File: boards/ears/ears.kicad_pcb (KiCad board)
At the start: 2 copper layers, 5 parts, among them J1 Conn_01x02_Male, U1 AZ1117-3.3, U2 SPX2920T-5.0_TO263, U3 ESP32-WROOM-32D

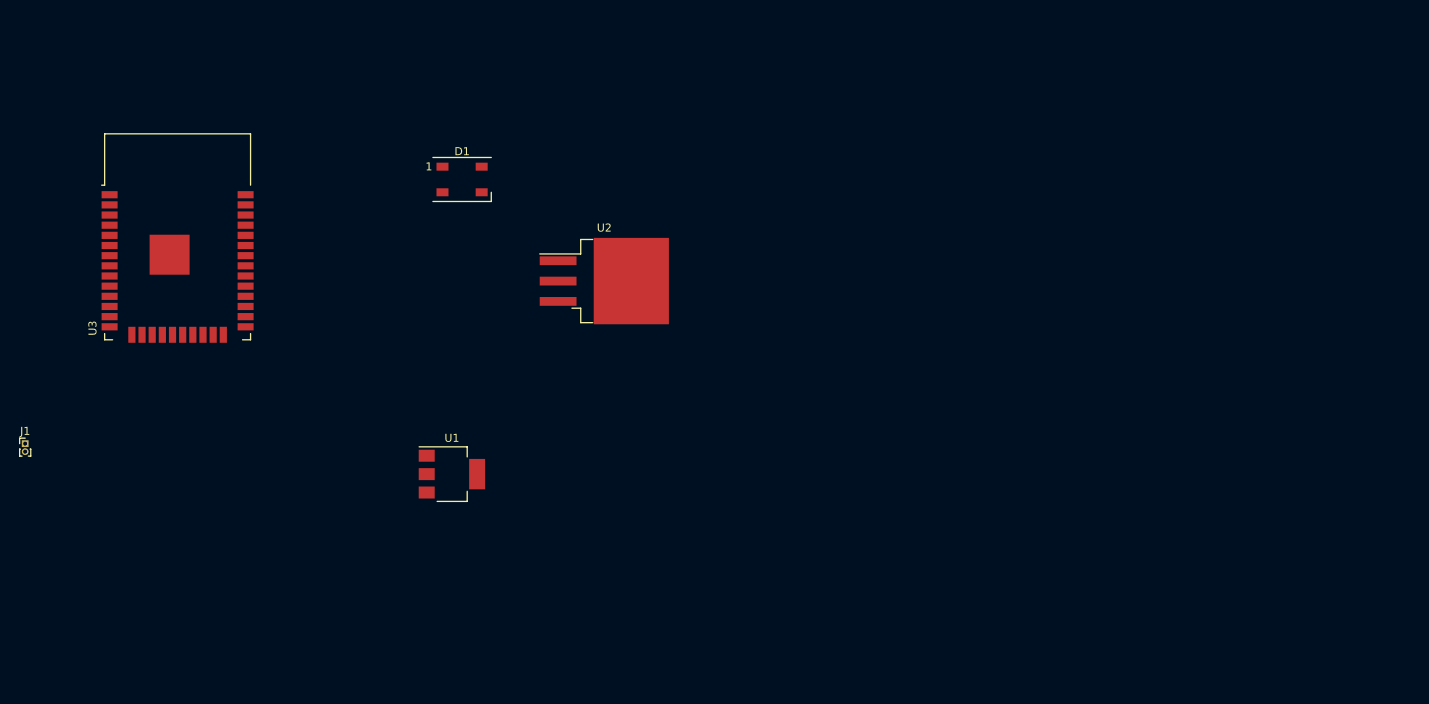
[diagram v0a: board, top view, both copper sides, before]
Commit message: - Ear boards V1
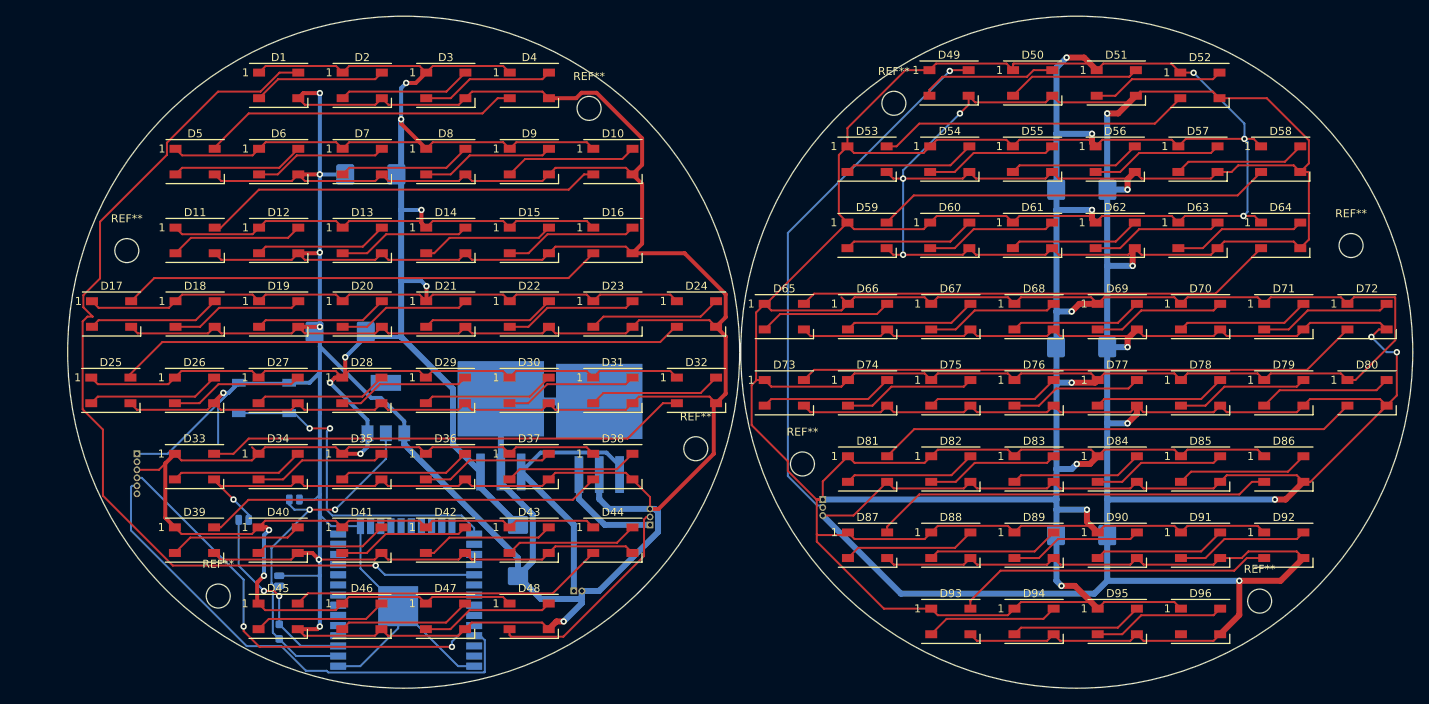
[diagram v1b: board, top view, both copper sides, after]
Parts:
- added C1: 0.1uF, Capacitor_SMD:C_0504_1310Metric_Pad0.83x1.28mm_HandSolder, B.Cu at (43.8, 79.4)
- added C2: 10uF, Capacitor_SMD:C_0504_1310Metric_Pad0.83x1.28mm_HandSolder, B.Cu at (50.2, 76.8)
- added C3: 0.1uF, Capacitor_SMD:C_0504_1310Metric_Pad0.83x1.28mm_HandSolder, B.Cu at (48.3, 87.0)
- added C4: 470uF, Capacitor_Tantalum_SMD:CP_EIA-7343-15_Kemet-W_Pad2.25x2.55mm_HandSolder, B.Cu at (55.9, 55.9)
- added C5: 470uF, Capacitor_Tantalum_SMD:CP_EIA-7343-15_Kemet-W_Pad2.25x2.55mm_HandSolder, B.Cu at (78.1, 83.2)
- added C6: 470uF, Capacitor_Tantalum_SMD:CP_EIA-7343-15_Kemet-W_Pad2.25x2.55mm_HandSolder, B.Cu at (59.7, 36.2)
- added C7: 470uF, Capacitor_Tantalum_SMD:CP_EIA-7343-15_Kemet-W_Pad2.25x2.55mm_HandSolder, B.Cu at (148.6, 57.8)
- added C8: 470uF, Capacitor_Tantalum_SMD:CP_EIA-7343-15_Kemet-W_Pad2.25x2.55mm_HandSolder, B.Cu at (148.6, 38.1)
- added C9: 470uF, Capacitor_Tantalum_SMD:CP_EIA-7343-15_Kemet-W_Pad2.25x2.55mm_HandSolder, B.Cu at (148.6, 81.3)
- added D10: WS2812B, LED_SMD:LED_WS2812B_PLCC4_5.0x5.0mm_P3.2mm, F.Cu at (90.0, 34.6)
- added D11: WS2812B, LED_SMD:LED_WS2812B_PLCC4_5.0x5.0mm_P3.2mm, F.Cu at (37.8, 44.5)
- added D12: WS2812B, LED_SMD:LED_WS2812B_PLCC4_5.0x5.0mm_P3.2mm, F.Cu at (48.2, 44.5)
- added D13: WS2812B, LED_SMD:LED_WS2812B_PLCC4_5.0x5.0mm_P3.2mm, F.Cu at (58.6, 44.5)
- added D14: WS2812B, LED_SMD:LED_WS2812B_PLCC4_5.0x5.0mm_P3.2mm, F.Cu at (69.1, 44.5)
- added D15: WS2812B, LED_SMD:LED_WS2812B_PLCC4_5.0x5.0mm_P3.2mm, F.Cu at (79.5, 44.5)
- added D16: WS2812B, LED_SMD:LED_WS2812B_PLCC4_5.0x5.0mm_P3.2mm, F.Cu at (90.0, 44.5)
- added D17: WS2812B, LED_SMD:LED_WS2812B_PLCC4_5.0x5.0mm_P3.2mm, F.Cu at (27.3, 53.6)
- added D18: WS2812B, LED_SMD:LED_WS2812B_PLCC4_5.0x5.0mm_P3.2mm, F.Cu at (37.8, 53.6)
- added D19: WS2812B, LED_SMD:LED_WS2812B_PLCC4_5.0x5.0mm_P3.2mm, F.Cu at (48.2, 53.6)
- added D2: WS2812B, LED_SMD:LED_WS2812B_PLCC4_5.0x5.0mm_P3.2mm, F.Cu at (58.6, 25.1)
- added D20: WS2812B, LED_SMD:LED_WS2812B_PLCC4_5.0x5.0mm_P3.2mm, F.Cu at (58.6, 53.6)
- added D21: WS2812B, LED_SMD:LED_WS2812B_PLCC4_5.0x5.0mm_P3.2mm, F.Cu at (69.1, 53.6)
- added D22: WS2812B, LED_SMD:LED_WS2812B_PLCC4_5.0x5.0mm_P3.2mm, F.Cu at (79.5, 53.6)
- added D23: WS2812B, LED_SMD:LED_WS2812B_PLCC4_5.0x5.0mm_P3.2mm, F.Cu at (90.0, 53.6)
- added D24: WS2812B, LED_SMD:LED_WS2812B_PLCC4_5.0x5.0mm_P3.2mm, F.Cu at (100.4, 53.6)
- added D25: WS2812B, LED_SMD:LED_WS2812B_PLCC4_5.0x5.0mm_P3.2mm, F.Cu at (27.2, 63.2)
- added D26: WS2812B, LED_SMD:LED_WS2812B_PLCC4_5.0x5.0mm_P3.2mm, F.Cu at (37.7, 63.2)
- added D27: WS2812B, LED_SMD:LED_WS2812B_PLCC4_5.0x5.0mm_P3.2mm, F.Cu at (48.1, 63.2)
- added D28: WS2812B, LED_SMD:LED_WS2812B_PLCC4_5.0x5.0mm_P3.2mm, F.Cu at (58.6, 63.2)
- added D29: WS2812B, LED_SMD:LED_WS2812B_PLCC4_5.0x5.0mm_P3.2mm, F.Cu at (69.0, 63.2)
- added D3: WS2812B, LED_SMD:LED_WS2812B_PLCC4_5.0x5.0mm_P3.2mm, F.Cu at (69.1, 25.1)
- added D30: WS2812B, LED_SMD:LED_WS2812B_PLCC4_5.0x5.0mm_P3.2mm, F.Cu at (79.5, 63.2)
- added D31: WS2812B, LED_SMD:LED_WS2812B_PLCC4_5.0x5.0mm_P3.2mm, F.Cu at (90.0, 63.2)
- added D32: WS2812B, LED_SMD:LED_WS2812B_PLCC4_5.0x5.0mm_P3.2mm, F.Cu at (100.4, 63.2)
- added D33: WS2812B, LED_SMD:LED_WS2812B_PLCC4_5.0x5.0mm_P3.2mm, F.Cu at (37.7, 72.7)
- added D34: WS2812B, LED_SMD:LED_WS2812B_PLCC4_5.0x5.0mm_P3.2mm, F.Cu at (48.1, 72.7)
- added D35: WS2812B, LED_SMD:LED_WS2812B_PLCC4_5.0x5.0mm_P3.2mm, F.Cu at (58.6, 72.7)
- added D36: WS2812B, LED_SMD:LED_WS2812B_PLCC4_5.0x5.0mm_P3.2mm, F.Cu at (69.0, 72.7)
- added D37: WS2812B, LED_SMD:LED_WS2812B_PLCC4_5.0x5.0mm_P3.2mm, F.Cu at (79.5, 72.7)
- added D38: WS2812B, LED_SMD:LED_WS2812B_PLCC4_5.0x5.0mm_P3.2mm, F.Cu at (90.0, 72.7)
- added D39: WS2812B, LED_SMD:LED_WS2812B_PLCC4_5.0x5.0mm_P3.2mm, F.Cu at (37.7, 81.9)
- added D4: WS2812B, LED_SMD:LED_WS2812B_PLCC4_5.0x5.0mm_P3.2mm, F.Cu at (79.5, 25.1)
- added D40: WS2812B, LED_SMD:LED_WS2812B_PLCC4_5.0x5.0mm_P3.2mm, F.Cu at (48.1, 81.9)
- added D41: WS2812B, LED_SMD:LED_WS2812B_PLCC4_5.0x5.0mm_P3.2mm, F.Cu at (58.6, 81.9)
- added D42: WS2812B, LED_SMD:LED_WS2812B_PLCC4_5.0x5.0mm_P3.2mm, F.Cu at (69.0, 81.9)
- added D43: WS2812B, LED_SMD:LED_WS2812B_PLCC4_5.0x5.0mm_P3.2mm, F.Cu at (79.5, 81.9)
- added D44: WS2812B, LED_SMD:LED_WS2812B_PLCC4_5.0x5.0mm_P3.2mm, F.Cu at (90.0, 81.9)
- added D45: WS2812B, LED_SMD:LED_WS2812B_PLCC4_5.0x5.0mm_P3.2mm, F.Cu at (48.1, 91.4)
- added D46: WS2812B, LED_SMD:LED_WS2812B_PLCC4_5.0x5.0mm_P3.2mm, F.Cu at (58.6, 91.4)
- added D47: WS2812B, LED_SMD:LED_WS2812B_PLCC4_5.0x5.0mm_P3.2mm, F.Cu at (69.0, 91.4)
- added D48: WS2812B, LED_SMD:LED_WS2812B_PLCC4_5.0x5.0mm_P3.2mm, F.Cu at (79.5, 91.4)
- added D49: WS2812B, LED_SMD:LED_WS2812B_PLCC4_5.0x5.0mm_P3.2mm, F.Cu at (132.0, 24.8)
- added D5: WS2812B, LED_SMD:LED_WS2812B_PLCC4_5.0x5.0mm_P3.2mm, F.Cu at (37.8, 34.6)
- added D50: WS2812B, LED_SMD:LED_WS2812B_PLCC4_5.0x5.0mm_P3.2mm, F.Cu at (142.4, 24.8)
- added D51: WS2812B, LED_SMD:LED_WS2812B_PLCC4_5.0x5.0mm_P3.2mm, F.Cu at (152.9, 24.8)
- added D52: WS2812B, LED_SMD:LED_WS2812B_PLCC4_5.0x5.0mm_P3.2mm, F.Cu at (163.3, 25.1)
- added D53: WS2812B, LED_SMD:LED_WS2812B_PLCC4_5.0x5.0mm_P3.2mm, F.Cu at (121.7, 34.3)
- added D54: WS2812B, LED_SMD:LED_WS2812B_PLCC4_5.0x5.0mm_P3.2mm, F.Cu at (132.1, 34.3)
- added D55: WS2812B, LED_SMD:LED_WS2812B_PLCC4_5.0x5.0mm_P3.2mm, F.Cu at (142.4, 34.3)
- added D56: WS2812B, LED_SMD:LED_WS2812B_PLCC4_5.0x5.0mm_P3.2mm, F.Cu at (152.8, 34.3)
- added D57: WS2812B, LED_SMD:LED_WS2812B_PLCC4_5.0x5.0mm_P3.2mm, F.Cu at (163.1, 34.3)
- added D58: WS2812B, LED_SMD:LED_WS2812B_PLCC4_5.0x5.0mm_P3.2mm, F.Cu at (173.4, 34.3)
- added D59: WS2812B, LED_SMD:LED_WS2812B_PLCC4_5.0x5.0mm_P3.2mm, F.Cu at (121.7, 43.8)
- added D6: WS2812B, LED_SMD:LED_WS2812B_PLCC4_5.0x5.0mm_P3.2mm, F.Cu at (48.2, 34.6)
- added D60: WS2812B, LED_SMD:LED_WS2812B_PLCC4_5.0x5.0mm_P3.2mm, F.Cu at (132.1, 43.8)
- added D61: WS2812B, LED_SMD:LED_WS2812B_PLCC4_5.0x5.0mm_P3.2mm, F.Cu at (142.4, 43.8)
- added D62: WS2812B, LED_SMD:LED_WS2812B_PLCC4_5.0x5.0mm_P3.2mm, F.Cu at (152.8, 43.8)
- added D63: WS2812B, LED_SMD:LED_WS2812B_PLCC4_5.0x5.0mm_P3.2mm, F.Cu at (163.1, 43.8)
- added D64: WS2812B, LED_SMD:LED_WS2812B_PLCC4_5.0x5.0mm_P3.2mm, F.Cu at (173.4, 43.8)
- added D65: WS2812B, LED_SMD:LED_WS2812B_PLCC4_5.0x5.0mm_P3.2mm, F.Cu at (111.4, 54.0)
- added D66: WS2812B, LED_SMD:LED_WS2812B_PLCC4_5.0x5.0mm_P3.2mm, F.Cu at (121.8, 54.0)
- added D67: WS2812B, LED_SMD:LED_WS2812B_PLCC4_5.0x5.0mm_P3.2mm, F.Cu at (132.2, 54.0)
- added D68: WS2812B, LED_SMD:LED_WS2812B_PLCC4_5.0x5.0mm_P3.2mm, F.Cu at (142.6, 54.0)
- added D69: WS2812B, LED_SMD:LED_WS2812B_PLCC4_5.0x5.0mm_P3.2mm, F.Cu at (153.0, 54.0)
- added D7: WS2812B, LED_SMD:LED_WS2812B_PLCC4_5.0x5.0mm_P3.2mm, F.Cu at (58.6, 34.6)
- added D70: WS2812B, LED_SMD:LED_WS2812B_PLCC4_5.0x5.0mm_P3.2mm, F.Cu at (163.4, 54.0)
- added D71: WS2812B, LED_SMD:LED_WS2812B_PLCC4_5.0x5.0mm_P3.2mm, F.Cu at (173.8, 54.0)
- added D72: WS2812B, LED_SMD:LED_WS2812B_PLCC4_5.0x5.0mm_P3.2mm, F.Cu at (184.2, 54.0)
- added D73: WS2812B, LED_SMD:LED_WS2812B_PLCC4_5.0x5.0mm_P3.2mm, F.Cu at (111.4, 63.5)
- added D74: WS2812B, LED_SMD:LED_WS2812B_PLCC4_5.0x5.0mm_P3.2mm, F.Cu at (121.8, 63.5)
- added D75: WS2812B, LED_SMD:LED_WS2812B_PLCC4_5.0x5.0mm_P3.2mm, F.Cu at (132.2, 63.5)
- added D76: WS2812B, LED_SMD:LED_WS2812B_PLCC4_5.0x5.0mm_P3.2mm, F.Cu at (142.6, 63.5)
- added D77: WS2812B, LED_SMD:LED_WS2812B_PLCC4_5.0x5.0mm_P3.2mm, F.Cu at (153.0, 63.5)
- added D78: WS2812B, LED_SMD:LED_WS2812B_PLCC4_5.0x5.0mm_P3.2mm, F.Cu at (163.4, 63.5)
- added D79: WS2812B, LED_SMD:LED_WS2812B_PLCC4_5.0x5.0mm_P3.2mm, F.Cu at (173.8, 63.5)
- added D8: WS2812B, LED_SMD:LED_WS2812B_PLCC4_5.0x5.0mm_P3.2mm, F.Cu at (69.1, 34.6)
- added D80: WS2812B, LED_SMD:LED_WS2812B_PLCC4_5.0x5.0mm_P3.2mm, F.Cu at (184.2, 63.5)
- added D81: WS2812B, LED_SMD:LED_WS2812B_PLCC4_5.0x5.0mm_P3.2mm, F.Cu at (121.8, 73.0)
- added D82: WS2812B, LED_SMD:LED_WS2812B_PLCC4_5.0x5.0mm_P3.2mm, F.Cu at (132.2, 73.0)
- added D83: WS2812B, LED_SMD:LED_WS2812B_PLCC4_5.0x5.0mm_P3.2mm, F.Cu at (142.6, 73.0)
- added D84: WS2812B, LED_SMD:LED_WS2812B_PLCC4_5.0x5.0mm_P3.2mm, F.Cu at (153.0, 73.0)
- added D85: WS2812B, LED_SMD:LED_WS2812B_PLCC4_5.0x5.0mm_P3.2mm, F.Cu at (163.4, 73.0)
- added D86: WS2812B, LED_SMD:LED_WS2812B_PLCC4_5.0x5.0mm_P3.2mm, F.Cu at (173.8, 73.0)
- added D87: WS2812B, LED_SMD:LED_WS2812B_PLCC4_5.0x5.0mm_P3.2mm, F.Cu at (121.8, 82.5)
- added D88: WS2812B, LED_SMD:LED_WS2812B_PLCC4_5.0x5.0mm_P3.2mm, F.Cu at (132.2, 82.5)
- added D89: WS2812B, LED_SMD:LED_WS2812B_PLCC4_5.0x5.0mm_P3.2mm, F.Cu at (142.6, 82.5)
- added D9: WS2812B, LED_SMD:LED_WS2812B_PLCC4_5.0x5.0mm_P3.2mm, F.Cu at (79.5, 34.6)
- added D90: WS2812B, LED_SMD:LED_WS2812B_PLCC4_5.0x5.0mm_P3.2mm, F.Cu at (153.0, 82.5)
- added D91: WS2812B, LED_SMD:LED_WS2812B_PLCC4_5.0x5.0mm_P3.2mm, F.Cu at (163.4, 82.5)
- added D92: WS2812B, LED_SMD:LED_WS2812B_PLCC4_5.0x5.0mm_P3.2mm, F.Cu at (173.8, 82.5)
- added D93: WS2812B, LED_SMD:LED_WS2812B_PLCC4_5.0x5.0mm_P3.2mm, F.Cu at (132.2, 92.1)
- added D94: WS2812B, LED_SMD:LED_WS2812B_PLCC4_5.0x5.0mm_P3.2mm, F.Cu at (142.6, 92.1)
- added D95: WS2812B, LED_SMD:LED_WS2812B_PLCC4_5.0x5.0mm_P3.2mm, F.Cu at (153.0, 92.1)
- added D96: WS2812B, LED_SMD:LED_WS2812B_PLCC4_5.0x5.0mm_P3.2mm, F.Cu at (163.4, 92.1)
- added J2: ESP32-Serial, Connector_PinHeader_1.00mm:PinHeader_1x06_P1.00mm_Horizontal, B.Cu at (30.5, 71.1)
- added J3: Conn_01x03_Male, Connector_PinHeader_1.00mm:PinHeader_1x03_P1.00mm_Horizontal, B.Cu at (116.2, 76.8)
- added J4: Conn_01x03_Male, Connector_PinHeader_1.00mm:PinHeader_1x03_P1.00mm_Horizontal, B.Cu at (94.6, 80.0)
- added R1: 10k, Resistor_SMD:R_0603_1608Metric_Pad0.98x0.95mm_HandSolder, B.Cu at (48.3, 93.3)
- added REF**: MountingHole_3mm, MountingHole:MountingHole_3mm, F.Cu at (170.8, 89.5)
- added REF**: MountingHole_3mm, MountingHole:MountingHole_3mm, F.Cu at (113.7, 72.4)
- added REF**: MountingHole_3mm, MountingHole:MountingHole_3mm, F.Cu at (182.2, 45.1)
- added REF**: MountingHole_3mm, MountingHole:MountingHole_3mm, F.Cu at (125.1, 27.3)
- added REF**: MountingHole_3mm, MountingHole:MountingHole_3mm, F.Cu at (29.2, 45.7)
- added REF**: MountingHole_3mm, MountingHole:MountingHole_3mm, F.Cu at (87.0, 27.9)
- added REF**: MountingHole_3mm, MountingHole:MountingHole_3mm, F.Cu at (100.3, 70.5)
- added REF**: MountingHole_3mm, MountingHole:MountingHole_3mm, F.Cu at (40.6, 88.9)
- added SW1: BOOT_MODE, Button_Switch_SMD:SW_SPST_TL3342, B.Cu at (46.4, 64.1)
- added U4: SPX2920T-5.0_TO263, Package_TO_SOT_SMD:TO-263-3_TabPin2, B.Cu at (88.3, 67.9)
- J1: value Conn_01x02_Male -> Power; footprint Connector_PinHeader_1.00mm:PinHeader_1x02_P1.00mm_Vertical -> Connector_PinHeader_1.00mm:PinHeader_1x02_P1.00mm_Horizontal; moved to B.Cu
- U1, U2, U3: moved to B.Cu
- moved J1 71.0 mm to (85.1, 88.3), turned to 270 degrees
- moved U3 51.2 mm to (64.1, 89.4)
- moved D1 25.8 mm to (48.2, 25.1)
- moved U2 22.2 mm to (76.0, 67.6), turned to 90 degrees
- moved U1 11.7 mm to (61.6, 65.4), turned to 90 degrees
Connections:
- net Net-(D1-Pad4) renamed /DATA_LED
- J1 pad 1: Net-(J1-Pad1) -> /V_BATT
- U1 pad 3: Net-(J1-Pad1) -> +5V
- U2 pad 1: Net-(J1-Pad1) -> /V_BATT
- U3 pad 25: Net-(U3-Pad25) -> /BOOT_MODE
- U3 pad 34: Net-(U3-Pad34) -> /RXD
- U3 pad 35: Net-(U3-Pad35) -> /TXD
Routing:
- net GND: track 0.00 -> 828.8 mm, vias 0 -> 9
- net /Sheet615F7669/5V_EARS2: track 0.00 -> 735.0 mm, vias 0 -> 11
- net /Sheet615F7669/GND_EARS2: track 0.00 -> 716.8 mm, vias 0 -> 12
- net +5V: track 0.00 -> 580.4 mm, vias 0 -> 9
- net /DATA_LED: track 0.00 -> 121.4 mm, vias 0 -> 1
- net Net-(D24-Pad2): track 0.00 -> 71.2 mm
- net Net-(D72-Pad2): track 0.00 -> 70.6 mm
- net /Sheet615F7669/DATA_LED_EARS2: track 0.00 -> 67.4 mm, vias 0 -> 1
- net /TXD: track 0.00 -> 63.4 mm
- net Net-(D80-Pad2): track 0.00 -> 60.6 mm
- net Net-(D32-Pad2): track 0.00 -> 60.5 mm
- net Net-(D16-Pad2): track 0.00 -> 60.3 mm
- net Net-(D64-Pad2): track 0.00 -> 60.2 mm
- net /RXD: track 0.00 -> 56.1 mm, vias 0 -> 2
- net Net-(D86-Pad2): track 0.00 -> 50.6 mm
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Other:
- board outline added: 168.1 x 84 mm
